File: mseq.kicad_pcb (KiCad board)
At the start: 2 copper layers, 113.7 x 67.6 mm, 88 parts, among them J1 Screen_I2C, J3 Conn_ARM_JTAG_SWD_10, SW1 RESET, SW2 ON/OFF, SW3 MS/SLAVE, SW4 BOOT, U1 SN74HCT125DR, U2 H11L1M, U3 AMS1117-3.3, U4 STM32F413CHUx, U5 CP2102N-Axx-xQFN20, U6 H11L1M, U7 W25Q16JVSS, U8 MB85RS256B, Y1 32.768kHz ±20ppm 6pF, Y2 25 MHz ±20ppm 18pF

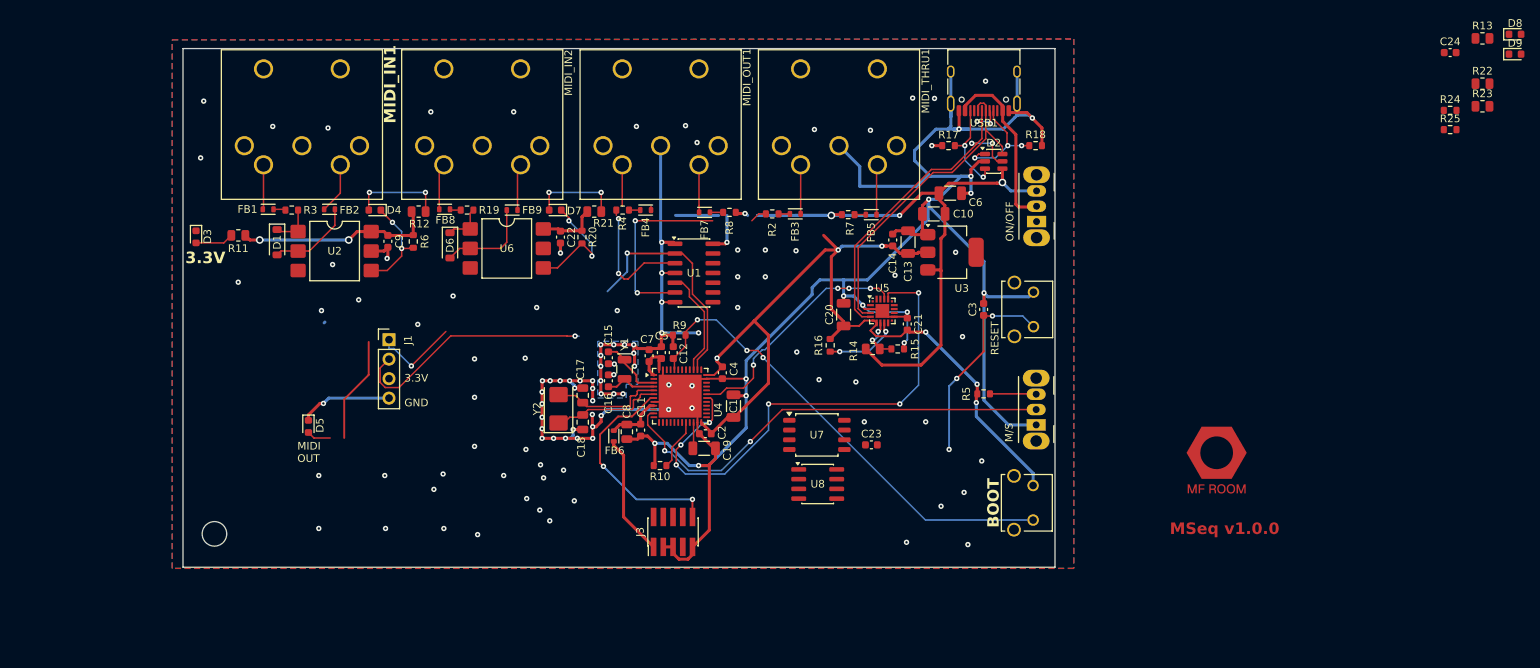
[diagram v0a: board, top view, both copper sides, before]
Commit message: PCB placement & routing WIP, board logos, DRC exclusions
Add res/ with the MF Room square logo (dark background removed) and the
OSHW logo, both transparent SVGs ready for Import Graphics onto silkscreen.

Exclude the two text_thickness DRC warnings on the OFF and SLV silkscreen
labels. Not genuinely thin strokes: KiCad's FreeType conversion emits a
self-intersecting outline for Geist's F and L, so the DRC deflate test
collapses a degenerate sliver. Reproducible with those glyphs alone at any
size and weight, clean in Helvetica, and gone with a static Geist-Bold.ttf
in place of the variable font.

Also J1 MPN/LCSC filled in.

Co-Authored-By: Claude Opus 5 <noreply@anthropic.com>
Claude-Session: https://claude.ai/code/session_014D6qtQcTakGg9PCa4hkr3z
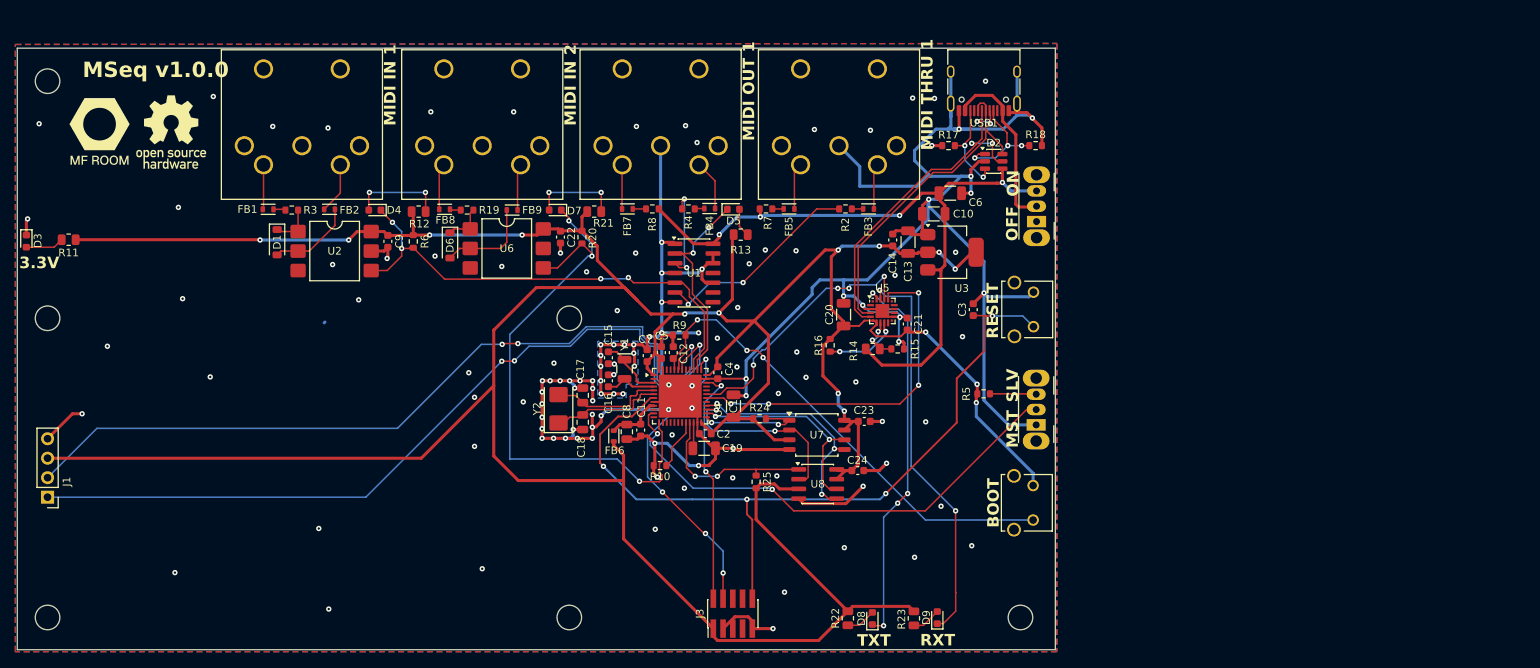
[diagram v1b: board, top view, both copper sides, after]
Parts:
- removed the REF** at (40.0, 111.5)
- added REF**: MountingHole_3.2mm_M3, MountingHole:MountingHole_3.2mm_M3, F.Cu at (18.2, 83.4)
- added REF**: MountingHole_3.2mm_M3, MountingHole:MountingHole_3.2mm_M3, F.Cu at (18.2, 122.4)
- added REF**: MountingHole_3.2mm_M3, MountingHole:MountingHole_3.2mm_M3, F.Cu at (86.2, 83.4)
- added REF**: MountingHole_3.2mm_M3, MountingHole:MountingHole_3.2mm_M3, F.Cu at (86.2, 122.4)
- added REF**: MountingHole_3.2mm_M3, MountingHole:MountingHole_3.2mm_M3, F.Cu at (18.2, 52.5)
- added REF**: MountingHole_3.2mm_M3, MountingHole:MountingHole_3.2mm_M3, F.Cu at (145.1, 122.4)
- MIDI IN 1: renamed from MIDI_IN1
- MIDI IN 2: renamed from MIDI_IN2
- MIDI OUT 1: renamed from MIDI_OUT1
- MIDI THRU 1: renamed from MIDI_THRU1
- moved D8 113.2 mm to (125.8, 122.5), turned to 90 degrees
- moved R22 108.1 mm to (122.5, 122.5), turned to -90 degrees
- moved D9 105.2 mm to (134.2, 122.4), turned to 90 degrees
- moved R25 101.4 mm to (110.6, 104.7), turned to -90 degrees
- moved R13 100.0 mm to (108.6, 72.5)
- moved R23 99.7 mm to (131.2, 122.5), turned to -90 degrees
- moved R24 98.6 mm to (111.0, 96.5)
- moved C24 94.5 mm to (123.8, 103.2), turned to 180 degrees
- moved D5 62.2 mm to (107.6, 69.2), turned to 0 degrees
- moved J1 49.0 mm to (18.2, 106.7), turned to 180 degrees
- moved D3 22.1 mm to (15.5, 73.3)
- moved R11 22.1 mm to (21.0, 73.2)
- moved J3 13.2 mm to (107.6, 121.9)
- moved FB5 10.7 mm to (114.9, 69.2)
- moved R7 10.7 mm to (111.9, 69.2)
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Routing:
- net +3.3V: track 171.4 -> 486.3 mm, vias 8 -> 15
- net /B6: track 11.4 -> 108.9 mm, vias 1 -> 3
- net /B7: track 32.5 -> 106.7 mm, vias 1 -> 3
- net /A3: track 16.3 -> 76.6 mm, vias 2 -> 3
- net /RXT: track 0.00 -> 52.2 mm, vias 0 -> 2
- net /TXT: track 0.00 -> 49.8 mm, vias 0 -> 4
- net /NRST: track 55.5 -> 102.6 mm, vias 5 -> 4
- net /SWCLOCK: track 0.00 -> 40.2 mm, vias 0 -> 4
- net /B3: track 28.2 -> 64.0 mm, vias 2 -> 4
- net /SWDIO: track 0.00 -> 31.2 mm, vias 0 -> 2
- net /MOSI: track 0.00 -> 30.2 mm, vias 0 -> 3
- net /SCK: track 0.00 -> 27.5 mm, vias 0 -> 2
- net /MISO: track 0.00 -> 24.5 mm, vias 0 -> 2
- net /CSFRAM: track 0.00 -> 22.3 mm, vias 0 -> 2
- net /A9: track 67.4 -> 45.8 mm, vias 6 -> 4
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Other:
- board size 113.7 x 67.6 mm -> 135.3 x 78.4 mm
- board text added: "MST"
- board text added: "OFF"
- board text added: "ON"
- board text added: "RXT"
- board text added: "SLV"
- board text added: "TXT"
- board text removed: "3.3V GND"
- board text removed: "M/S"
- board text removed: "MIDI OUT"
- board text removed: "ON/OFF"
